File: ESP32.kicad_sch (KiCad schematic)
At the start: 10 parts, among them J201 GPIO, J203 Conn_01x01, J302 Conn_01x02, U201 ESP32-WROOM-32E-N16

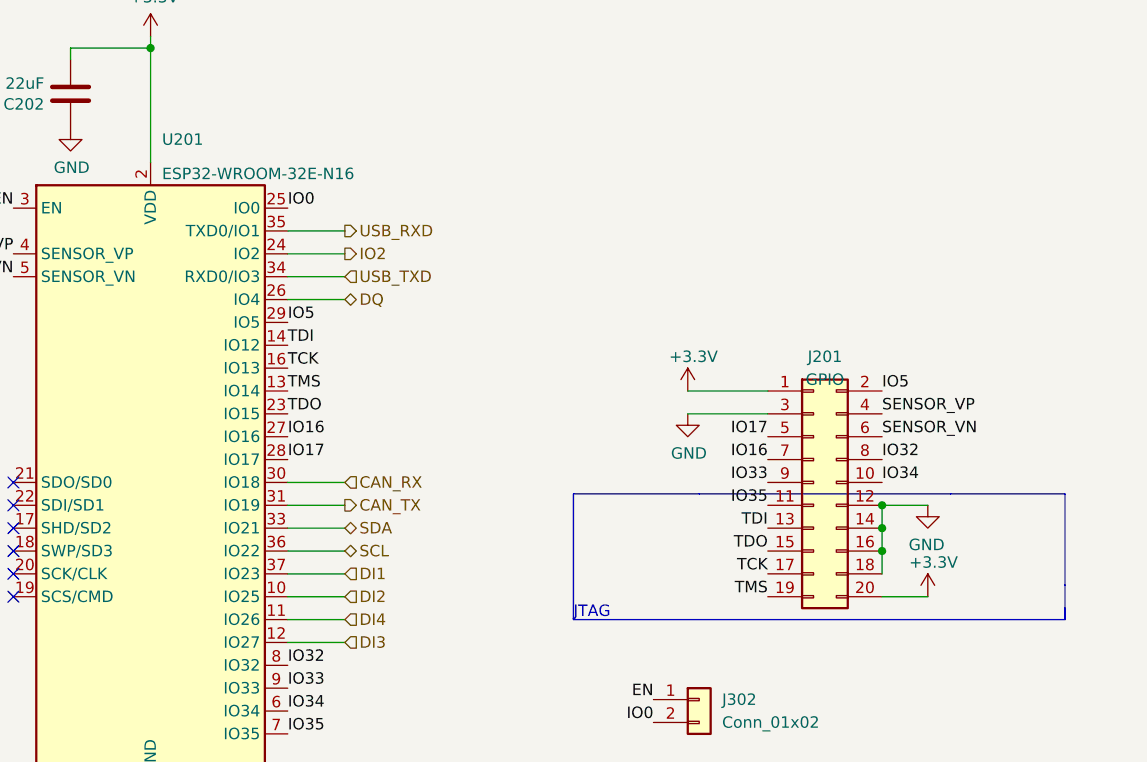
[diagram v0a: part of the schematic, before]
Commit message: Initial V1.0.0 Bluefin forked
Added ICM-42688-P 6-axis IMU
Added LM317 LDO for 6.4v or 5v MHU supply (selectable via jumper)
Added External LED's for IO2 (Pin 24) and 3.3v
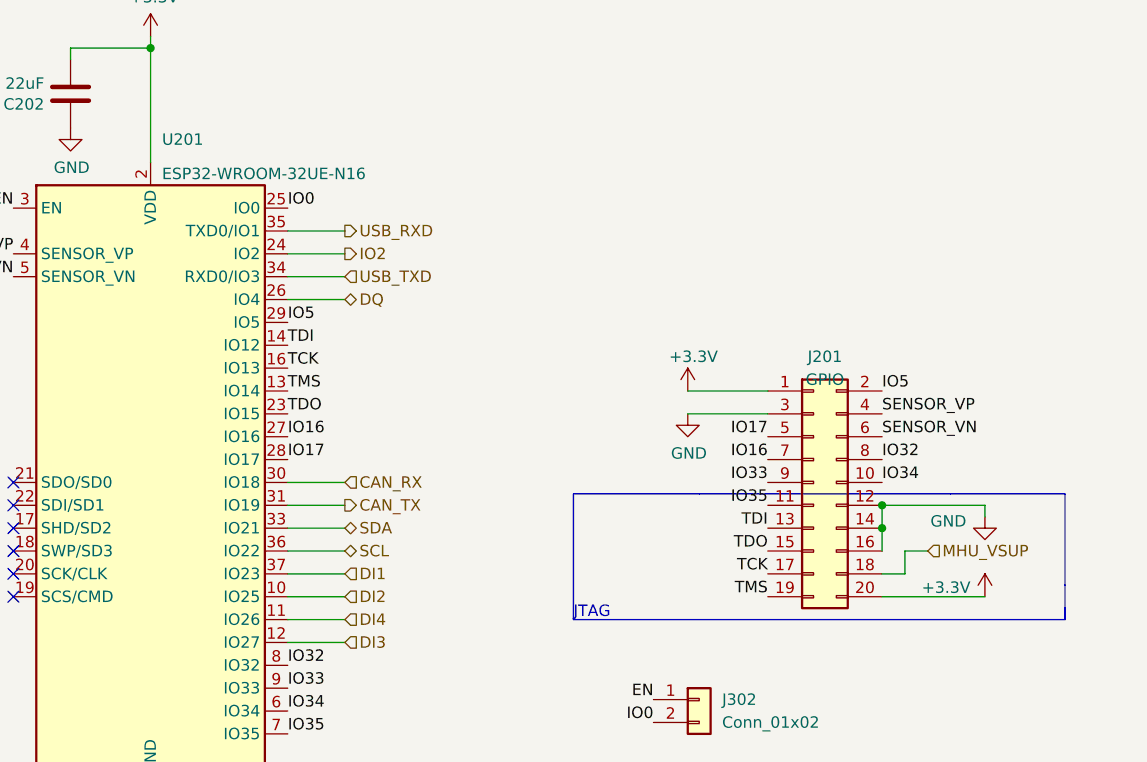
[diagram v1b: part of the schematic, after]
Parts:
- U201: value ESP32-WROOM-32E-N16 -> ESP32-WROOM-32UE-N16; footprint RF_Module:ESP32-WROOM-32 -> RF_Module:ESP32-WROOM-32UE; LCSC C701343 -> C701346
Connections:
- net GND: no longer J201.18 (Pin_18)
- new net MHU_VSUP: J201.18 (Pin_18)

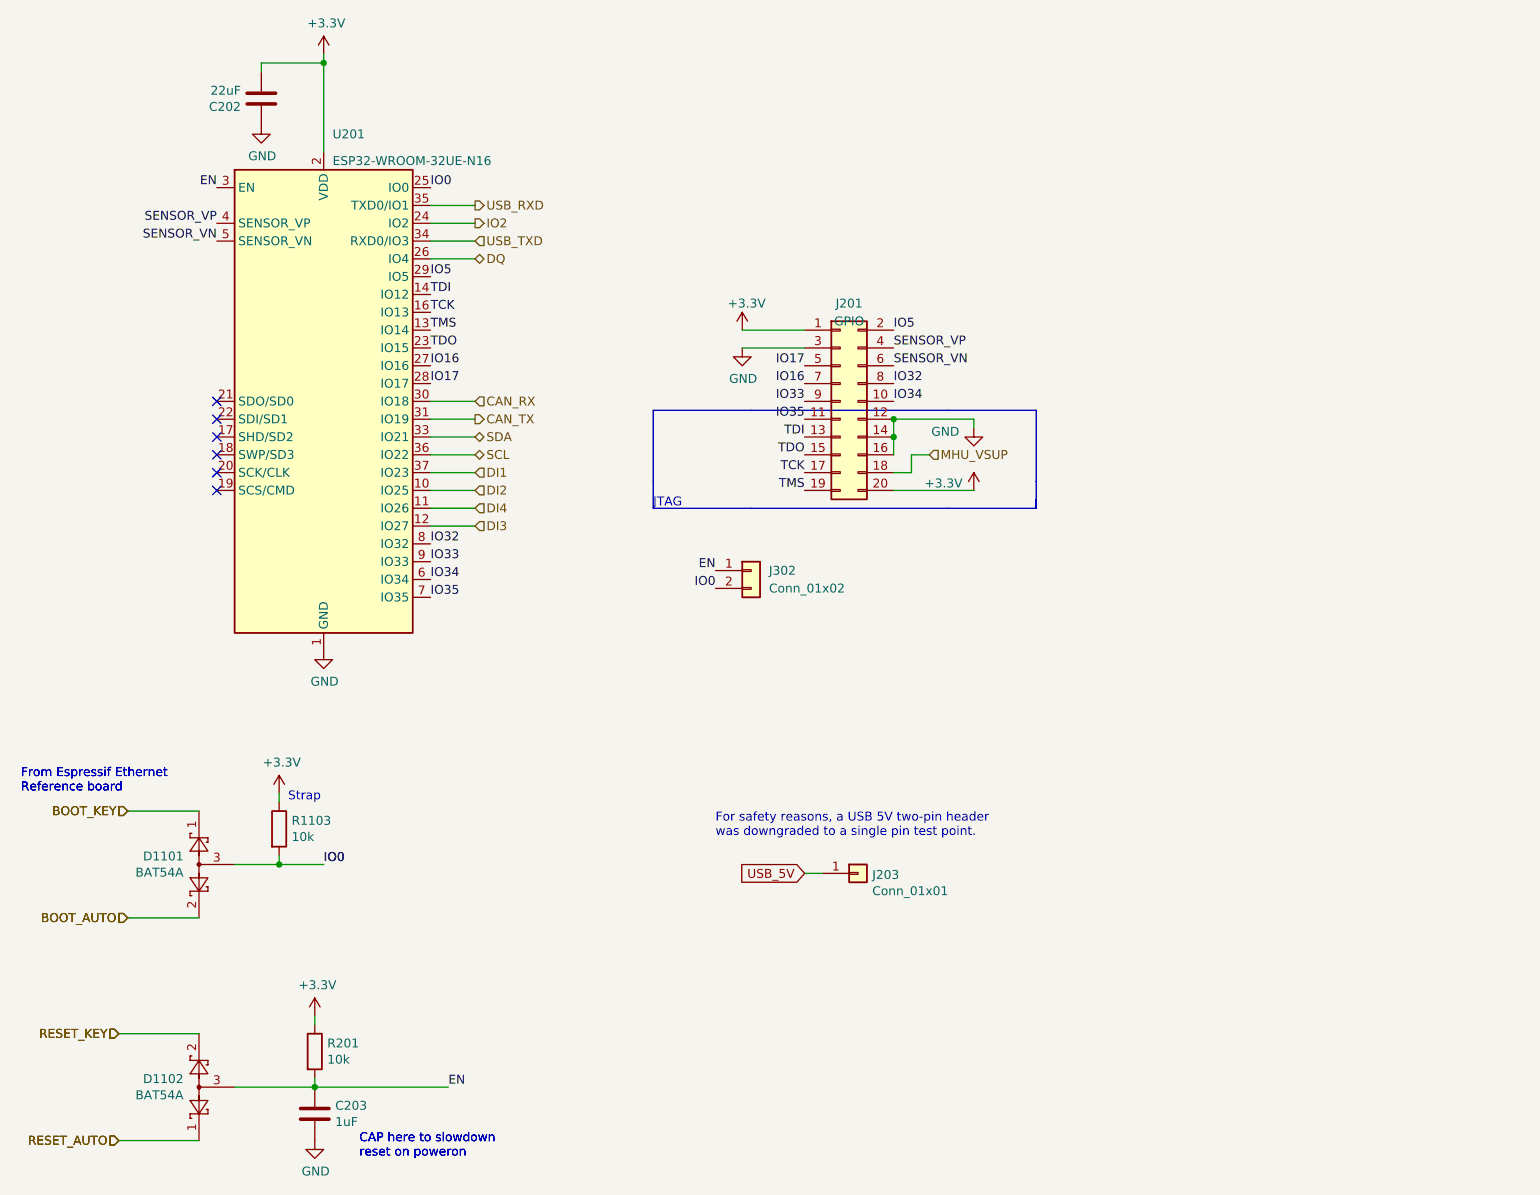
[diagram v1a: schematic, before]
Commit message: Added RS485/RS233 (NMEA 01830) chip
Added SP3485EN RS485 bi-directional driver with a GPIO toggle for changing input - output direction.

Connected to GPIO pin header
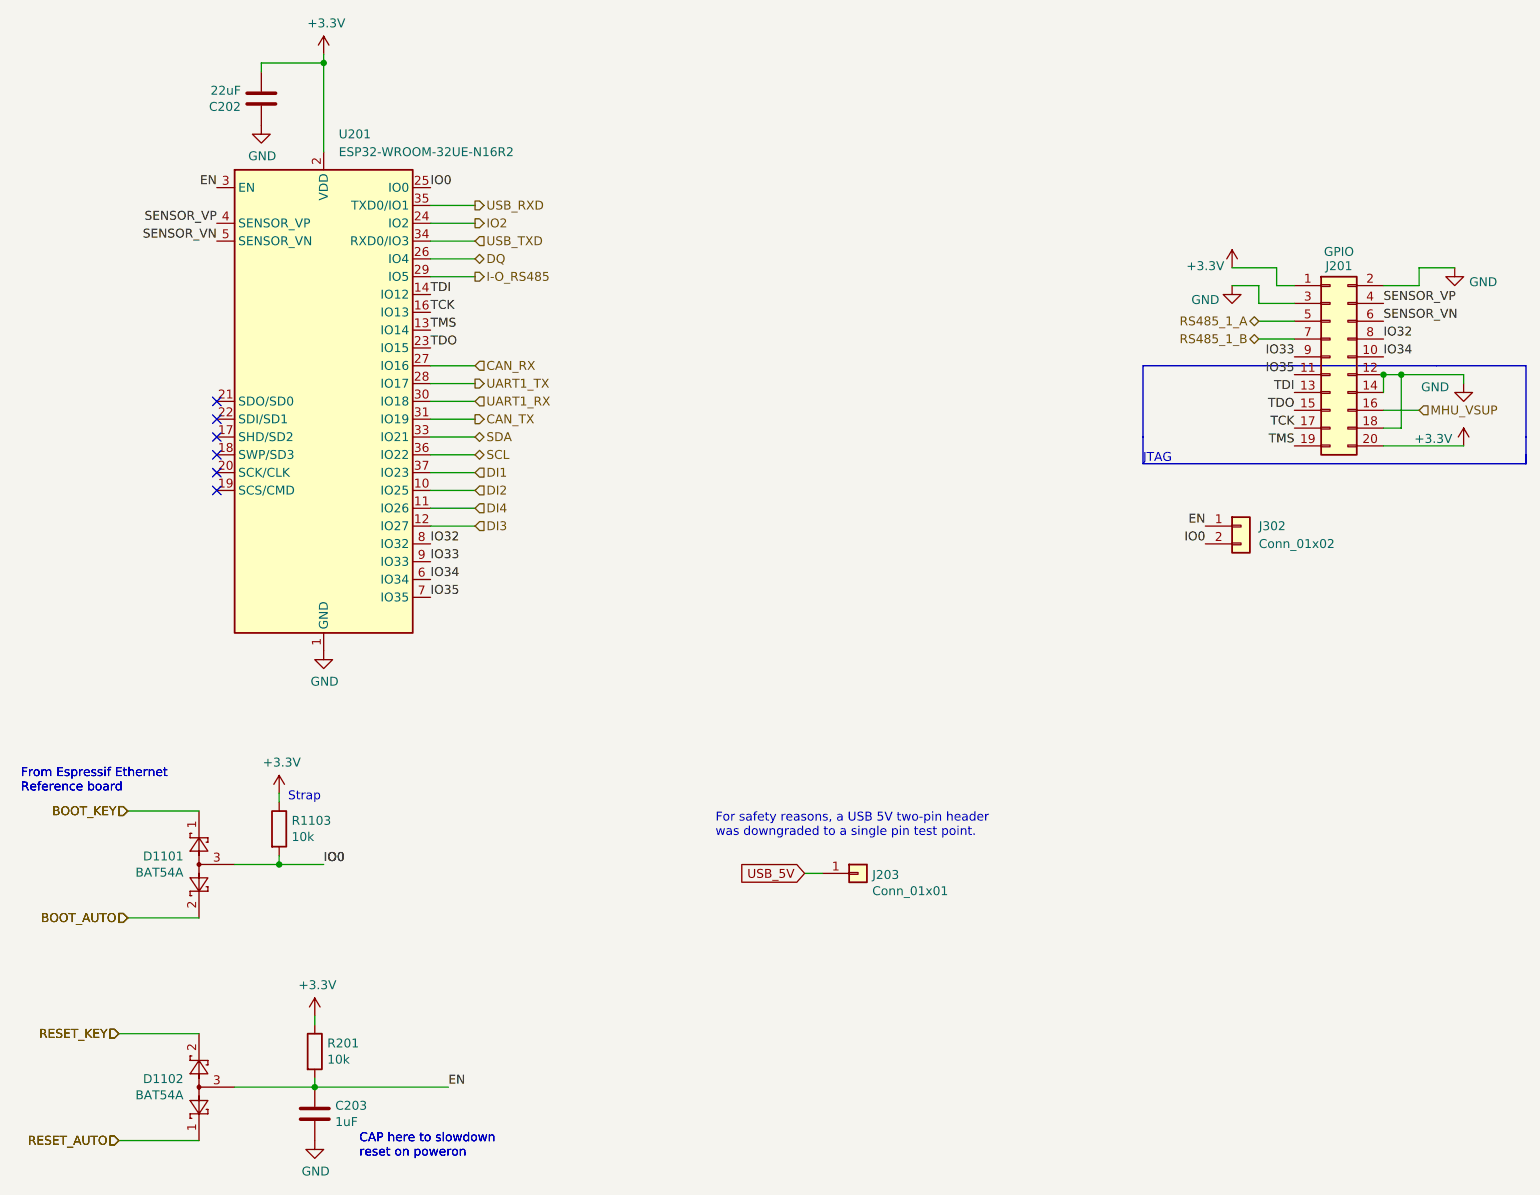
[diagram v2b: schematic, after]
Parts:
- J201: LCSC (none) -> C492427
- U201: value ESP32-WROOM-32UE-N16 -> ESP32-WROOM-32UE-N16R2
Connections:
- net CAN_RX: now also U201.27 (IO16); no longer U201.30 (IO18)
- net GND: now also J201.18 (Pin_18), J201.2 (Pin_2); no longer J201.16 (Pin_16)
- net MHU_VSUP: now also J201.16 (Pin_16); no longer J201.18 (Pin_18)
- net IO16 renamed RS485_1_B
- net RS485_1_B: no longer U201.27 (IO16)
- net IO17 renamed RS485_1_A
- net RS485_1_A: no longer U201.28 (IO17)
- net IO5 renamed I-O_RS485
- net I-O_RS485: no longer J201.2 (Pin_2)
- new net UART1_RX: U201.30 (IO18)
- new net UART1_TX: U201.28 (IO17)
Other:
- moved on the sheet: J201, J302

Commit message: Changed to ESP32-S3-WROOM-1U
Added ESP32-S3-WROOM-1U-N16R2  and updated all routing and pin assignments.

Added USB-OTG connected via JST-PH
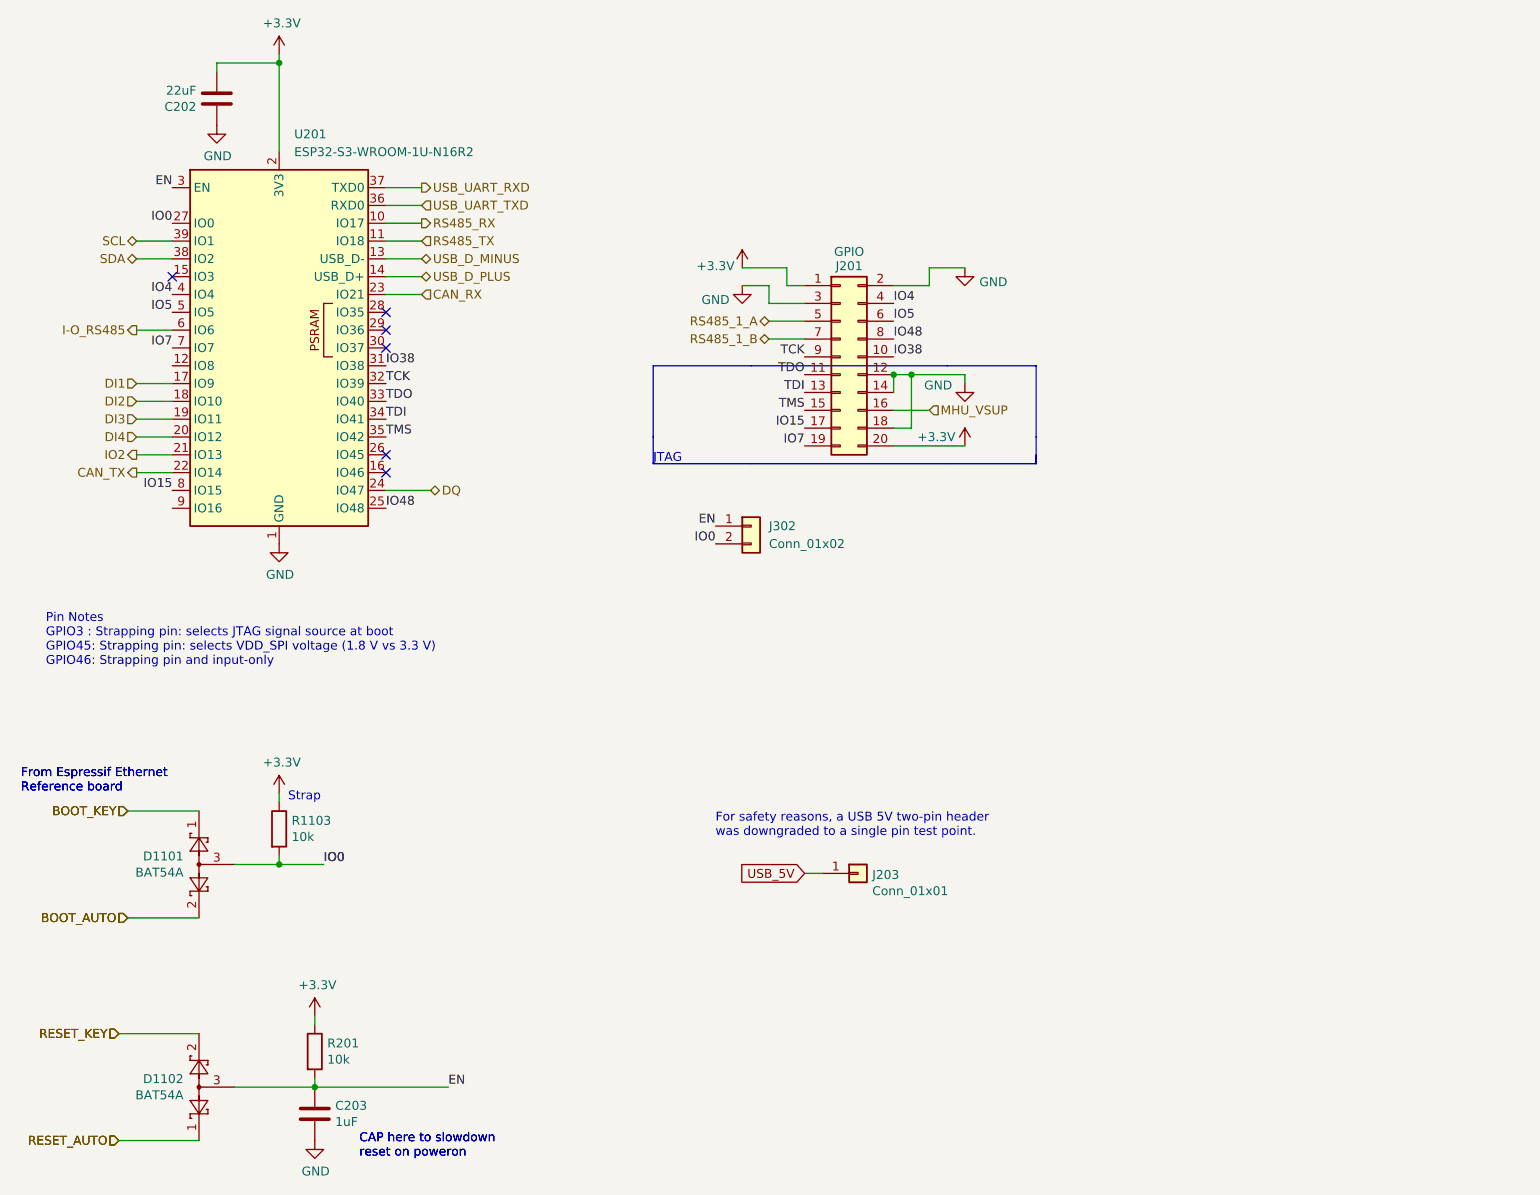
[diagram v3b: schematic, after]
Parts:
- removed U201: ESP32-WROOM-32UE-N16R2, RF_Module:ESP32-WROOM-32UE, symbol RF_Module:ESP32-WROOM-32
- added U201: ESP32-S3-WROOM-1U-N16R2, RF_Module:ESP32-S3-WROOM-1U, symbol RF_Module:ESP32-S3-WROOM-1
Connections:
- net IO33 is gone; now on net TCK: J201.9 (Pin_9)
- net IO35 is gone; now on net TDO: J201.11 (Pin_11)
- net +3.3V: now also U201.2 (3V3)
- net CAN_RX: now also U201.23 (IO21)
- net CAN_TX: now also U201.22 (IO14)
- net DI1: now also U201.17 (IO9)
- net DI2: now also U201.18 (IO10)
- net DI3: now also U201.19 (IO11)
- net DI4: now also U201.20 (IO12)
- net DQ: now also U201.24 (IO47)
- net EN: now also U201.3 (EN)
- net GND: now also U201.1 (GND), U201.40 (GND), U201.41 (GND)
- net I-O_RS485: now also U201.6 (IO6)
- net IO0: now also U201.27 (IO0)
- net IO2: now also U201.21 (IO13)
- net SCL: now also U201.39 (IO1)
- net SDA: now also U201.38 (IO2)
- net TCK: now also U201.32 (IO39); no longer J201.17 (Pin_17)
- net TDI: now also U201.34 (IO41)
- net TDO: now also U201.33 (IO40); no longer J201.15 (Pin_15)
- net TMS: now also J201.15 (Pin_15), U201.35 (IO42); no longer J201.19 (Pin_19)
- net IO32 renamed IO48
- net IO48: now also U201.25 (IO48)
- net IO34 renamed IO38
- net IO38: now also U201.31 (IO38)
- net SENSOR_VN renamed IO5
- net IO5: now also U201.5 (IO5)
- net SENSOR_VP renamed IO4
- net IO4: now also U201.4 (IO4)
- new net IO15: J201.17 (Pin_17), U201.8 (IO15)
- new net IO7: J201.19 (Pin_19), U201.7 (IO7)
- new net RS485_RX: U201.10 (IO17)
- new net RS485_TX: U201.11 (IO18)
- new net USB_D_MINUS: U201.13 (USB_D-)
- new net USB_D_PLUS: U201.14 (USB_D+)
- new net USB_UART_RXD: U201.37 (TXD0)
- new net USB_UART_TXD: U201.36 (RXD0)
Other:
- note added: "Pin Notes GPIO3 : Strapping pin: selects JTAG signal source at boot GPIO45: Strapping pin: selects VDD_SPI voltage (1.8 V vs 3.3 V) GPIO46: Strapping pin and input-only"
- moved on the sheet: C202, J201, J302

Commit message: Renames IO2 to IO13 for onboard LED
The original label "IO2" was incorrect and has been updated to "IO13"
to reflect the intended signal.
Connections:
- net IO2 renamed IO13
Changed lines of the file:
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@@
 		)
 	)
-	(hierarchical_label "IO2"
+	(hierarchical_label "IO13"
 		(shape output)
 		(at 38.1 81.28 180)

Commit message: Net renaming and Silkscreen tidy ups
The UART / Serial naming convention is revised for more consistency
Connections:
- net RS485_RX renamed UART1_TX
- net RS485_TX renamed UART1_RX
- net USB_UART_RXD renamed UART0_TX
- net USB_UART_TXD renamed UART0_RX
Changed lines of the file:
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@@
 		)
 	)
-	(hierarchical_label "RS485_RX"
+	(hierarchical_label "UART1_TX"
 		(shape output)
 		(at 78.74 48.26 0)
@@
 		)
 	)
-	(hierarchical_label "RS485_TX"
+	(hierarchical_label "UART1_RX"
 		(shape input)
 		(at 78.74 50.8 0)
@@
 		)
 	)
-	(hierarchical_label "USB_UART_RXD"
+	(hierarchical_label "UART0_TX"
 		(shape output)
 		(at 78.74 43.18 0)
@@
 		)
 	)
-	(hierarchical_label "USB_UART_TXD"
+	(hierarchical_label "UART0_RX"
 		(shape input)
 		(at 78.74 45.72 0)

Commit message: Changed MCU to ESP32-S3-WROOM-1U-N16R8
ESP32-S3-WROOM-1U-N16R8 has 8 MB of Octal PSRAM
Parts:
- U201: value ESP32-S3-WROOM-1U-N16R2 -> ESP32-S3-WROOM-1U-N16R8; LCSC C3013945 -> C3013946
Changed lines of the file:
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@@
 			)
 		)
-		(property "Value" "ESP32-S3-WROOM-1U-N16R2"
+		(property "Value" "ESP32-S3-WROOM-1U-N16R8"
 			(at 60.5633 38.1 0)
 			(effects
@@
 			)
 		)
-		(property "LCSC" "C3013945"
+		(property "LCSC" "C3013946"
 			(at 58.42 66.04 0)
 			(effects

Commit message: Moved ESP32-S3 + larger pin headers
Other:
- company: Hat Labs Ltd -> Fifty One North Limited
- title: Hat Labs Marine Engine & Tank interface (HALMET) -> Bluefin Marine Processor
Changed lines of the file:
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@@
 	(paper "A4")
 	(title_block
-		(title "Hat Labs Marine Engine & Tank interface (HALMET)")
-		(date "2024-01-18")
-		(rev "1.0.1")
-		(company "Hat Labs Ltd")
-		(comment 1 "https://creativecommons.org/licenses/by-sa/4.0")
-		(comment 2 "To view a copy of this license, visit ")
-		(comment 3 "HALMET is licensed under CC BY-SA 4.0.")
+		(title "Bluefin Marine Processor")
+		(date "2026-01-08")
+		(rev "1.0.0")
+		(company "Fifty One North Limited")
+		(comment 1 "https://creativecommons.org/licenses/by-sa/4.0/")
+		(comment 2 "Bluefin is licensed under CC BY-SA 4.0")
+		(comment 3 "Modifications © 2026 Fiftyone North Ltd.")
+		(comment 4 "Based on an original design by Hat Labs Ltd.")
 	)
 	(text "CAP here to slowdown \nreset on poweron"
